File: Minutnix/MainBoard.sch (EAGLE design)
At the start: 140 parts, among them IC1 MEGA8-AI, IC10 TPIC6C596PW, IC11 TPIC6C596PW, IC12 TPIC6C596PW, IC13 TPIC6C596PW, IC2 TPIC6C596PW, IC3 TPIC6C596PW, IC4 TPIC6C596PW, IC5 TPIC6C596PW, IC6 TP4056, IC8 FT230XS, IC9 SC4503, Q4 32.768kHz, T1 DMN3024LSD, X1 FH12-12S-0.5SH

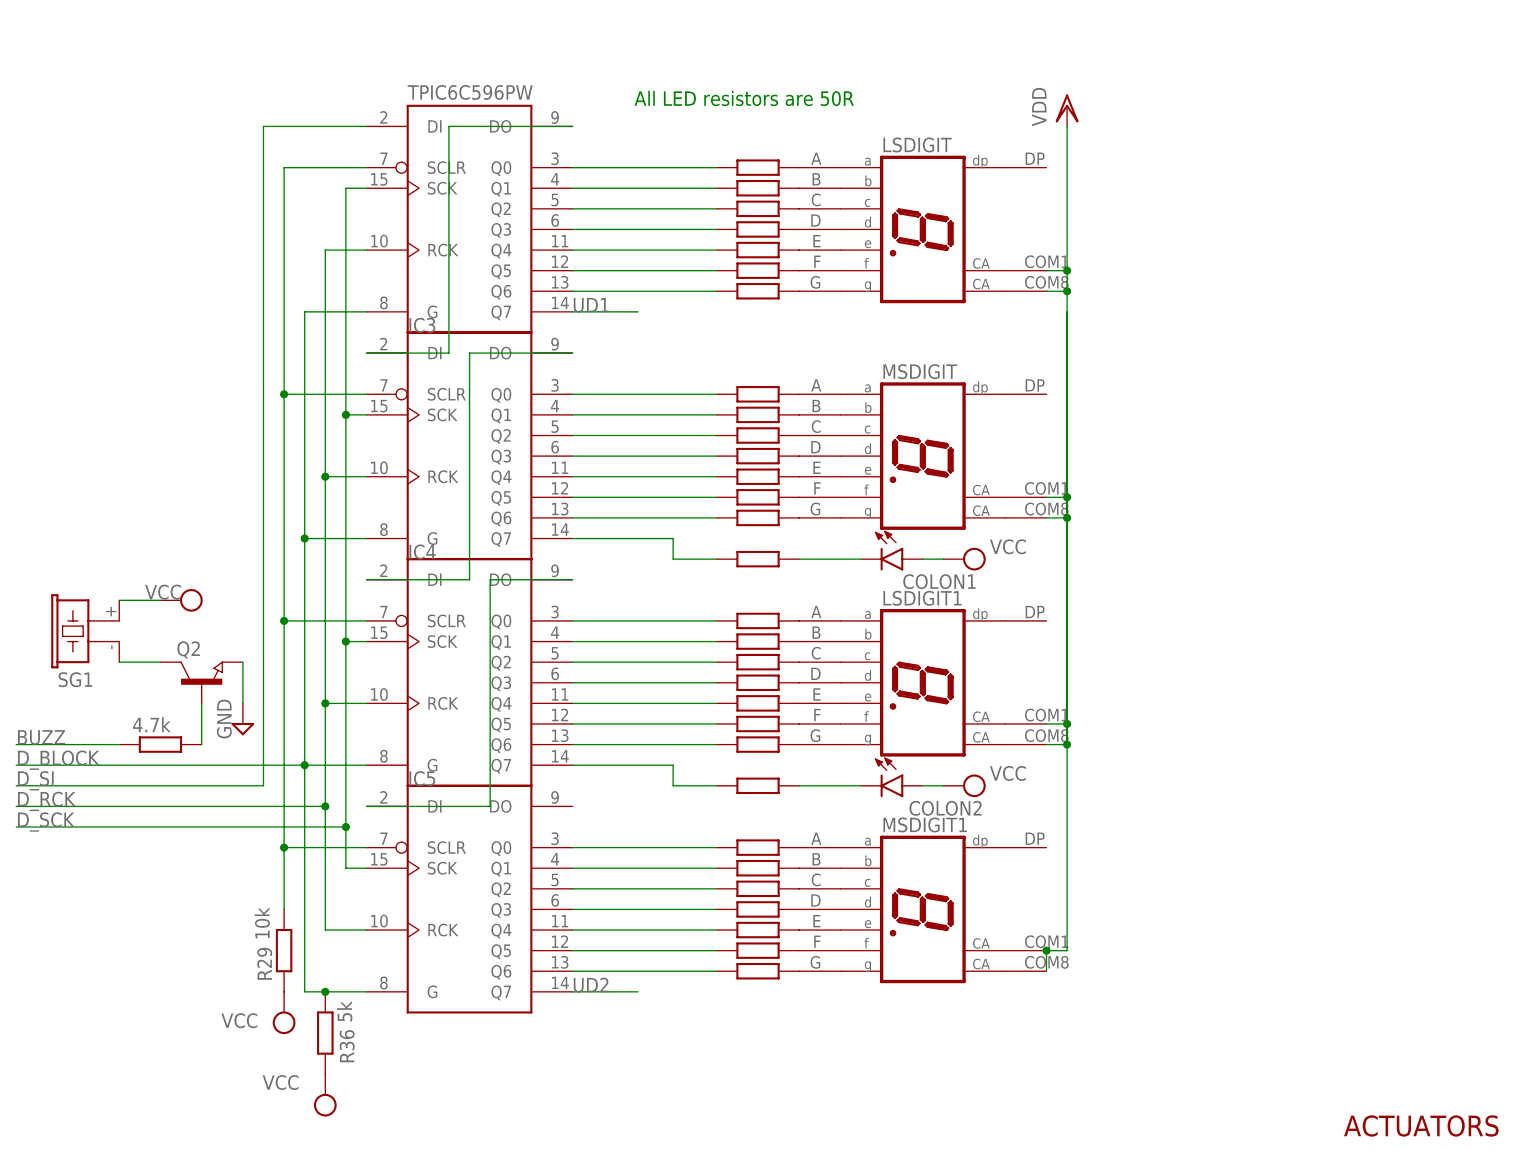
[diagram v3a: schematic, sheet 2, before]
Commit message: Major board changes
Remake of interface upper board + layout
Majior corrections in mainboard - correct models, cables, connectors, ft232 and more. Also more libraries.
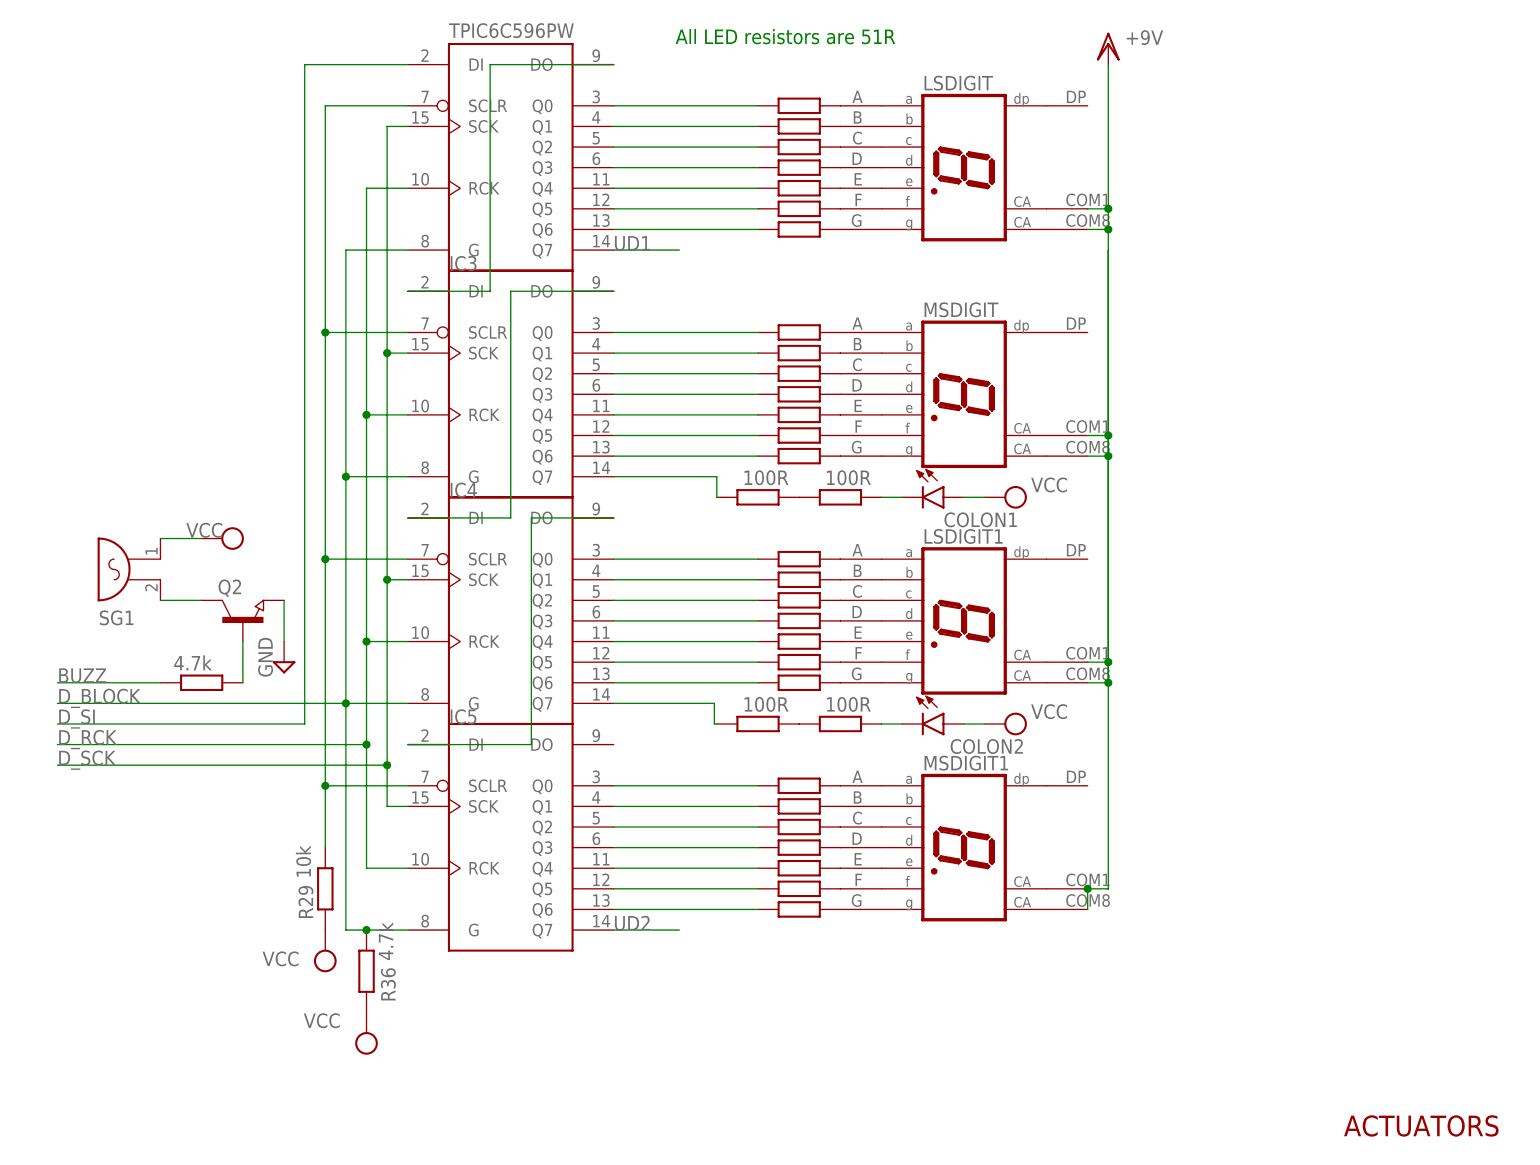
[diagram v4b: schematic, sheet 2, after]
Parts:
- removed C18, C23: 100n, capacitor-wima:C2.5/2
- removed C19, C20: 47p, capacitor-wima:C2.5/2
- removed C21: 4.7u, rcl:CPOL-EU140CLH-1010
- removed C22: 10n, capacitor-wima:C2.5/2
- removed C33: 100nF, rcl:CPOL-EU140CLH-1010
- removed G1: CRAA, battery:CRAA
- removed IC8: FT230XS, ftdi:FT230XS
- removed L2: BLM15HB121SN1, inductors:BLM15HB121SN1
- removed MICROUSB: MICRO-USB-RECEPTACLE47589-0001, con-molex-usb:MICRO-USB-RECEPTACLE47589-0001
- removed PROGRAMMING: SKHMPSE010, switch:SKHMPSE010
- removed R32: 47k, rcl:POTENTIOMETER_PT-10
- removed R58: 4.7k, rcl:R-EU_R1206
- removed R60: 4.7k, rcl:R-EU_01005
- removed R62, R63: 220, rcl:R-EU_01005
- added C1, C10, C2, C4: 100n, rcl:C-EUC0603
- added C3: 4.7u, rcl:C-EUC3216
- added IC7: FT232RL, ftdi:FT232RL
- added JP12, JP13, JP14, JP15, JP16, JP17, JP18, JP19, JP20: (no value), pinhead:PINHD-1X1
- added R65, R66: 100R, rcl:R-EU_R0603
- added X2, X3: 87438-03, con-molex:87438-03
- C29, C30: device capacitor-wima:C2.5/2 -> rcl:C-EUC0603
- C31: device rcl:CPOL-EU140CLH-1010 -> rcl:CPOL-EU153CLV-0810
- C5, C6, C7, C8, C9: value 0.1uF -> 100n; device rcl:CPOL-EU140CLH-1010 -> rcl:C-EUC0603
- L1: device inductor-neosid:MS42 -> inductors:DR73
- PHOTORES: value A1050_09 -> VT90N1; device photo-elements:A1050_09 -> photo-elements:VT90N1
- Q4: device crystal:CRYSTALTC26V -> crystal_clock:CRYSTAL-32.768KHZSMD-2X6
- R1, R10, R11, R12, R13, R14, R15, R16, R17, R18, R19, R2, R20, R21, R22, R23, R24, R25, R26, R27, R28, R29, R3, R30, R4, R5, R56, R6, R7, R8, R9: device rcl:R-EU_R1206 -> rcl:R-EU_R0603
- R31, R33, R42, R43, R44, R61: device rcl:R-EU_01005 -> rcl:R-EU_R0603
- R34, R35: value 200 -> 100R; device rcl:R-EU_R1206 -> rcl:R-EU_R0603
- R36: value 5k -> 4.7k; device rcl:R-EU_R1206 -> rcl:R-EU_R0603
- R45, R46: value 27R -> 4.7k; device rcl:R-EU_R1206 -> rcl:R-EU_R0603
- R47, R48: value 270 -> 100; device rcl:R-EU_R1206 -> rcl:R-EU_R0603
- R49, R50: value 10k -> 100R; device rcl:R-EU_R1206 -> rcl:R-EU_R0603
- R51, R52: value 10k -> 100; device rcl:R-EU_R1206 -> rcl:R-EU_R0603
- R57: value 7.05k -> (none); device rcl:R-EU_R1206 -> rcl:R-TRIMM3296Y
- R59: value 4.7k -> 100; device rcl:R-EU_01005 -> rcl:R-EU_R0603
- R64: value 220 -> 100; device rcl:R-EU_01005 -> rcl:R-EU_R0603
- RXLED, TXLED: device led:LED5MM -> led:LEDCHIPLED_0603
- SG1: value F/CM12P -> F/HGP; device buzzer:F/CM12P -> buzzer:F/HGP
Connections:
- removed net N$1: C11.2, G1.+, IC6.BAT, R40.1, S1.P
- removed net N$103: IC8.USBDM, R45.2
- removed net N$108: C13.1, G1.-, T1B.S, U$2.GND
- removed net N$114: R47.2, RXLED.C
- removed net N$115: IC8.CBUS2, R47.1
- removed net N$116: R48.2, TXLED.C
- removed net N$117: IC8.CBUS1, R48.1
- removed net N$120: COLON2.C, R35.1
- removed net N$37 (its old number): MSDIGIT.B, R9.1
- removed net N$55: MSDIGIT1.E, R26.1
- removed net N$56: MSDIGIT1.F, R27.1
- removed net S_VCC?: PROGRAMMING.2.1, PROGRAMMING.2.2
- removed net UF1: IC8.CBUS0, JP9.1
- removed net UF2: IC8.CBUS3, JP10.1
- new net BATTERY+: C11.2, IC6.BAT, R40.1, S1.P, X3-1.S
- new net BATTERY-: C13.1, T1B.S, U$2.GND, X3-3.S
- new net BATTERY_S: JP20.1, X3-2.S
- new net CBUS2: IC7.CBUS2, JP17.1
- new net CBUS3: IC7.CBUS3, JP18.1
- new net CBUS4: IC7.CBUS4, JP19.1
- new net CTS: IC7.!CTS, JP10.1
- new net DCD: IC7.!DCD, JP15.1
- new net DI: JP16.1
- new net DSR: IC7.!DSR, JP12.1
- new net DTR: C10.2, IC7.!DTR
- new net FTRESET: IC7.!RESET, JP7.1
- new net GNDA: ATMEGA328P.GND, IC1.GND
- new net N$31: MSDIGIT1.B, R26.1
- new net N$32: MSDIGIT1.A, R27.1
- new net N$33: MSDIGIT.G, R8.1
- new net N$35: MSDIGIT.E, R10.1
- new net N$36: IC7.CBUS0, R66.2
- new net N$39: MSDIGIT.B, R13.1
- new net N$43: IC7.CBUS1, R65.2
- new net N$64: R66.1, TXLED.C
- new net N$74: R65.1, RXLED.C
- new net OSCO: IC7.OSCO, JP8.1
- new net RI: IC7.!RI
- new net RTS: IC7.!RTS, JP9.1
- net +3V3: now also C1.2, IC7.3V3OUT; no longer C23.2, IC8.!RESET, IC8.3V3OUT, IC8.VCCIO, R49.2, R50.2, R51.1, R52.2
- net +5V: now also C2.2, C3.1, IC7.VCC, IC7.VCCIO, X2-1.S; no longer C18.2, C21.+, IC8.VCC, L2.1, SPI_JUMPERS.5
- net AREF: now also C4.1; no longer C33.+, R57.1, R58.2
- net COUNTER: now also R46.2; no longer R60.2
- net GND: now also C1.1, C2.1, C3.2, C4.2, C5.2, C6.2, C7.2, C8.2, C9.2, IC7.GND, IC7.GND@1, IC7.GND@2, IC7.GND@A, IC7.TEST, X2-2.S; no longer ATMEGA328P.GND, C18.1, C19.2, C20.1, C21.-, C22.1, C23.1, C33.-, C5.-, C6.-, C7.-, C8.-, C9.-, IC1.GND, IC8.GND, IC8.GND@1, MICROUSB.5, MICROUSB.GND1, MICROUSB.GND2, MICROUSB.GND3, MICROUSB.GND4, PROGRAMMING.1.1, PROGRAMMING.1.2, PROGRAMMING.SH, R57.2, X1-12.1
- net LIGHT_SENS: now also R57.S; no longer R32.3
- net L_COUNTER: now also R52.2; no longer R62.2
- net L_WARNING: now also R47.2; no longer R63.2
- net N$10: now also R16.2; no longer R6.2
- net N$11: now also R15.2; no longer R7.2
- net N$12: now also R49.1, R50.2; no longer COLON1.C, R34.1
- net N$13: now also LSDIGIT1.G; no longer LSDIGIT.A
- net N$14: now also MSDIGIT1.E, R23.1; no longer C22.2, L2.2, MICROUSB.1
- net N$15: now also LSDIGIT1.F; no longer LSDIGIT.B
- net N$16: now also LSDIGIT1.E; no longer LSDIGIT.C
- net N$17: now also LSDIGIT1.D; no longer LSDIGIT.D
- net N$18: now also LSDIGIT1.C; no longer LSDIGIT.E
- net N$19: now also LSDIGIT1.B; no longer LSDIGIT.F
- net N$2: now also R49.2; no longer R34.2
- net N$21: now also MSDIGIT1.D, R24.1; no longer IC8.!RTS, R51.2
- net N$22: now also R27.2; no longer R22.2
- net N$23: now also MSDIGIT1.C, R25.1; no longer IC8.USBDP, R46.2
- net N$25: now also LSDIGIT1.A; no longer LSDIGIT.G
- net N$26: now also R51.1, X1-10.1; no longer R62.1, X1-8.1
- net N$28: now also R48.1; no longer R63.1
- net N$29: now also R59.1, X1-8.1; no longer R64.1, X1-10.1
- net N$3: now also MSDIGIT1.F, R22.1; no longer IC8.!CTS, R52.1
- net N$34: now also MSDIGIT.F, R9.1; no longer MSDIGIT.A, R8.1
- net N$38: now also R12.1; no longer R10.1
- net N$4: now also R14.2; no longer R8.2
- net N$40: now also MSDIGIT.A, R14.1; no longer MSDIGIT.E, R12.1
- net N$41: now also LSDIGIT.G, R15.1; no longer MSDIGIT.F, R13.1
- net N$42: now also LSDIGIT.F, R16.1; no longer MSDIGIT.G, R14.1
- net N$44: now also LSDIGIT.E, R17.1; no longer LSDIGIT1.A, R15.1
- net N$45: now also LSDIGIT.D, R18.1; no longer LSDIGIT1.B, R16.1
- net N$46: now also LSDIGIT.C, R19.1; no longer LSDIGIT1.C, R17.1
- net N$47: now also LSDIGIT.B, R20.1; no longer LSDIGIT1.D, R18.1
- net N$48: now also LSDIGIT.A, R21.1; no longer LSDIGIT1.E, R19.1
- net N$49: now also R34.2, R35.1; no longer LSDIGIT1.F, R20.1
- net N$5: now also R21.2; no longer R1.2
- net N$50: now also COLON1.C, R50.1; no longer LSDIGIT1.G, R21.1
- net N$51: now also COLON2.C, R34.1; no longer MSDIGIT1.A, R22.1
- net N$52: now also R51.2, R64.1; no longer MSDIGIT1.B, R23.1
- net N$53: now also R47.1, R48.2; no longer MSDIGIT1.C, R24.1
- net N$54: now also R52.1, R59.2; no longer MSDIGIT1.D, R25.1
- net N$58: now also R13.2; no longer R9.2
- net N$59: now also R12.2; no longer R10.2
- net N$6: now also R20.2; no longer R2.2
- net N$61: now also R10.2; no longer R12.2
- net N$62: now also R9.2; no longer R13.2
- net N$63: now also R8.2; no longer R14.2
- net N$67: now also R7.2; no longer R15.2
- net N$68: now also R6.2; no longer R16.2
- net N$69: now also R5.2; no longer R17.2
- net N$7: now also R19.2; no longer R3.2
- net N$70: now also R4.2; no longer R18.2
- net N$71: now also R3.2; no longer R19.2
- net N$72: now also R2.2; no longer R20.2
- net N$73: now also R1.2; no longer R21.2
- net N$75: now also R26.2; no longer R23.2
- net N$76: now also R25.2; no longer R24.2
- net N$77: now also R24.2; no longer R25.2
- net N$8: now also R18.2; no longer R4.2
- net N$9: now also R17.2; no longer R5.2
- net N$94: now also R23.2; no longer R26.2
- net N$95: now also R22.2; no longer R27.2
- net RESET: now also C10.1
- net RXD: now also IC7.TXD; no longer IC8.TXD, R49.1
- net S_VCC: now also SPI_JUMPERS.5
- net TXD: now also IC7.RXD; no longer IC8.RXD, R50.1
- net UD1: now also JP13.1; no longer JP6.1
- net UD2: now also JP14.1; no longer JP7.1
- net UP1: now also JP6.1; no longer JP8.1
- net USBDM: now also IC7.USBDM, X1-11.1; no longer C19.1, MICROUSB.2, R45.1
- net USBDP: now also IC7.USBDP, X1-12.1; no longer C20.2, MICROUSB.3, R46.1
- net VCC: now also C5.1, C6.1, C7.1, C8.1, C9.1, R45.1, R46.1, X2-3.S; no longer C5.+, C6.+, C7.+, C8.+, C9.+, R58.1, R59.1, R60.1, X1-11.1
- net VDD: now also R57.A; no longer R32.1
- net WARNING: now also R45.2; no longer R59.2
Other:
- note added: "AVCC Supply and AREF"
- note added: "All LED resistors are 51R"
- note removed: "AREF"
- note removed: "AVCC Supply"
- note removed: "All LED resistors are 50R"
- note removed: "Ferrite bead"
- note removed: "MICRO USB INPUT"
- note removed: "Programming"
- note removed: "RESET"
- moved on the sheet: C11, COLON1, COLON2, IC3, IC4, IC5, JP1, JP10, JP2, JP3, JP4, JP5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
